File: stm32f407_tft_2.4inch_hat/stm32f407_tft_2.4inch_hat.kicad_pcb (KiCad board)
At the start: 2 copper layers, 62.7 x 90.2 mm, 6 parts, among them P1 STM32F407-DISC P1, P2 STM32F407-DISC P2

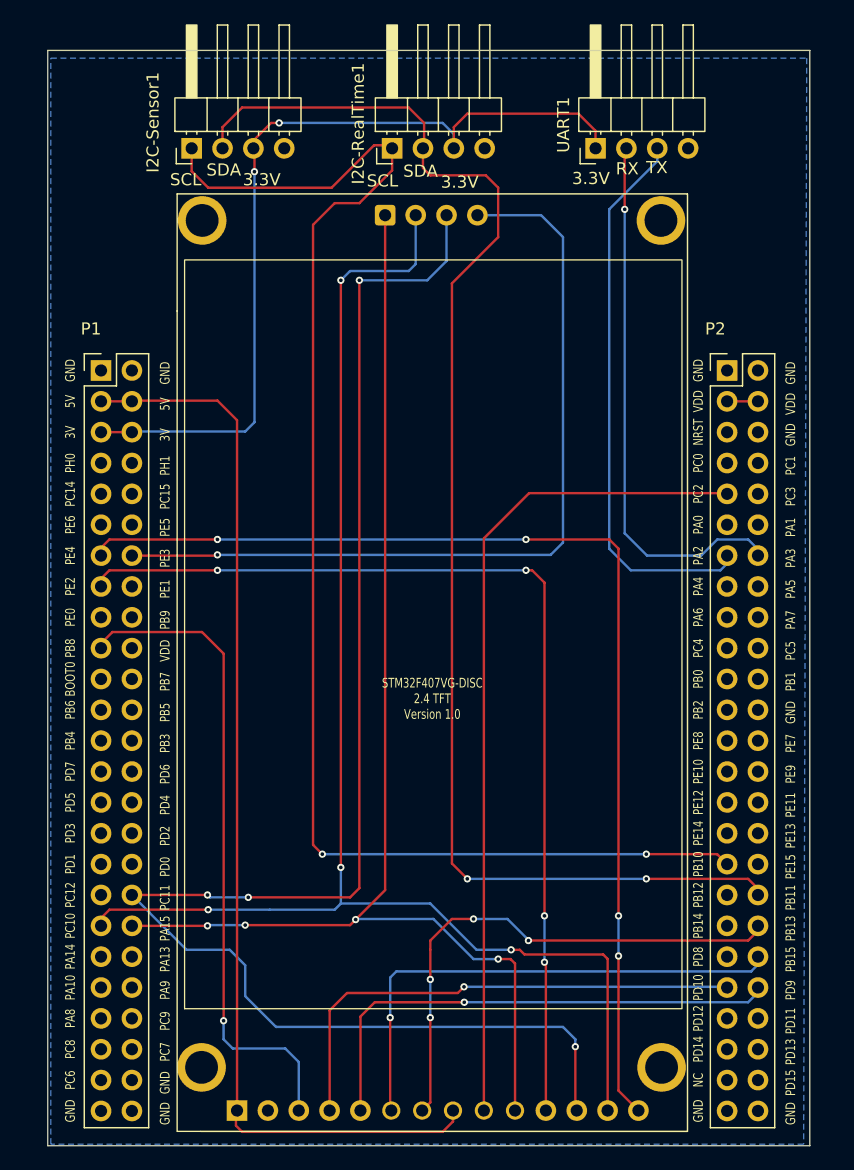
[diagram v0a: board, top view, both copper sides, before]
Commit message: Fix wrong labels in P1 and fix LCD SDcard pin order
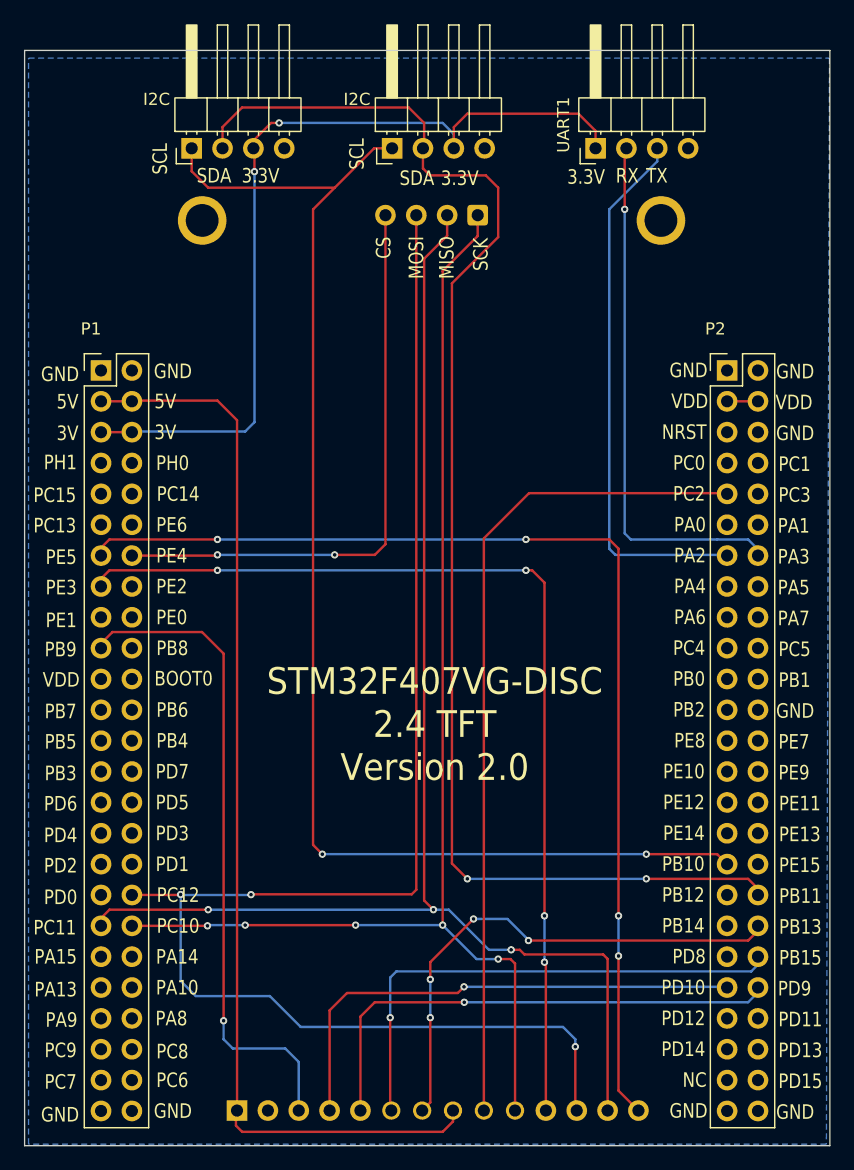
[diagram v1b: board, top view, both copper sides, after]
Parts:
- renumbered I2C-RealTime1 to I2C, I2C-Sensor1 to I2C
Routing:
- net /LCD_SD_CS: track 68.9 -> 48.3 mm, vias 1 -> 2
- net /I2C2_SCL: track 116.6 -> 109.9 mm
- net /LCD_SD_MISO: track 119.3 -> 115.2 mm, vias 4 -> 3
- net /LCD_SD_MOSI: track 129.8 -> 126.7 mm, vias 4 -> 3
- net /DBG_UART2_TX: track 46.7 -> 45.3 mm
- net /DBG_UART2_RX: track 46.2 -> 45.1 mm
- net /LCD_SCK: track 43.6 -> 42.6 mm
- net /LCD_SD_CLK: track 104.3 -> 104.6 mm, vias 4 -> 5
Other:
- board size 62.7 x 90.2 mm -> 66.3 x 90.2 mm
- board text added: "CS"
- board text added: "MISO"
- board text added: "MOSI"
- board text added: "PC13"
- board text added: "SCK"
- board text added: "STM32F407VG-DISC 2.4 TFT Version 2.0"
- board text removed: "STM32F407VG-DISC 2.4 TFT Version 1.0"
